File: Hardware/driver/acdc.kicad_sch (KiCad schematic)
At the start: 14 parts, among them J401 TBP02R2W-381-03BE, J402 Conn_01x02_Male

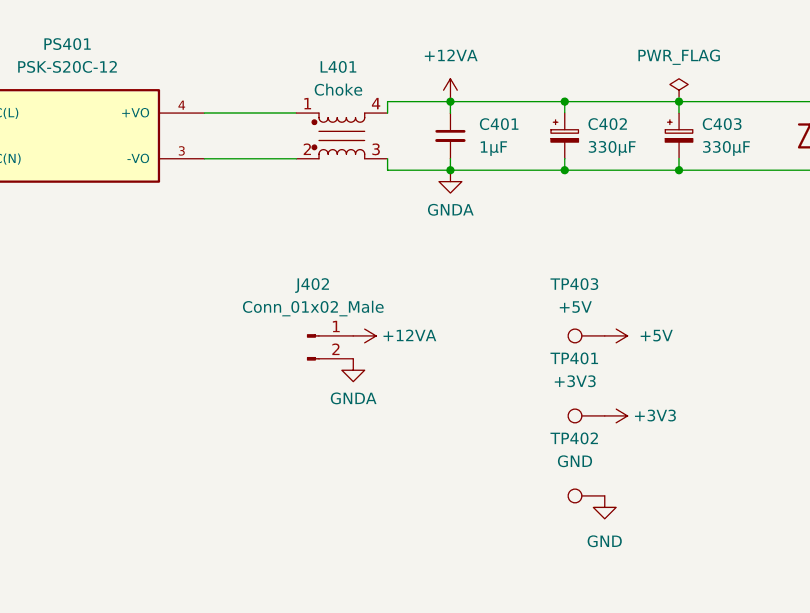
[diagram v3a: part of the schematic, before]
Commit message: Start work on remote VSense; driver board tweaks
- Use the DAC reference as the positive end of the null adjustment
  trimmers, rather than the +3V3 supply; this should make the adjustment
  actually useful and persistent rather than relying on the relationship
  between the 3V3 rail and the DAC's internal reference.

- Moved the 1Wire controller slightly to allow relocating the zero
  offset trimmer for the first channel

- Start work on remote VSense

  This works by selecting between either voltage sensing at the source
  terminals, or an external sense input connected to another set of
  terminals. These are switched by a latching relay (as to provide
  satisfying clicky noises) and then go into an op amp working as a
  differential amplifier; it performs a 50:1 gain (obviating the need
  for resistor dividers, and providing greater accuracy) and that then
  goes into the measurement ADC as normal.

  We have to still figure out how to drive the relay (probably just an
  IO expander?) and place those components on the board.
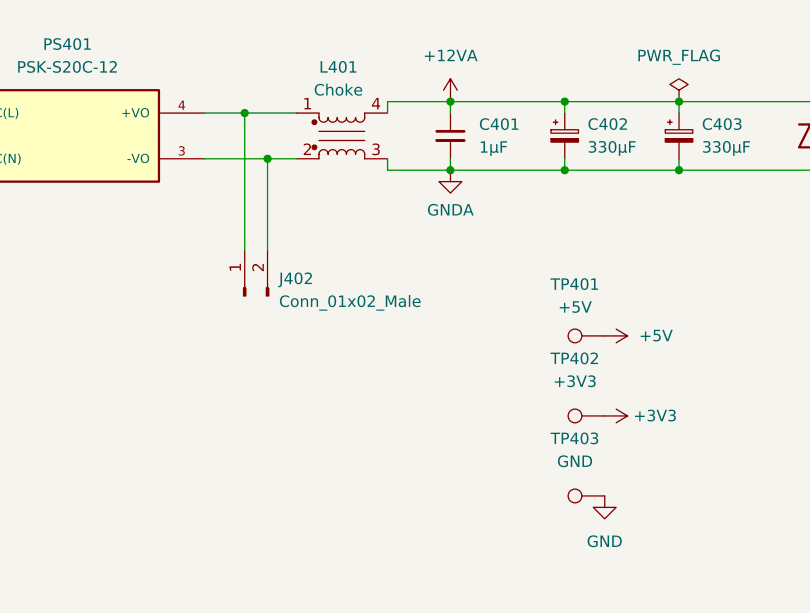
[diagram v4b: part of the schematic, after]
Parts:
- renumbered TP403 to TP401, TP401 to TP402, TP402 to TP403
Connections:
- net +12VA: no longer J402.1 (Pin_1)
- net GNDA: no longer J402.2 (Pin_2)
- net at L401.2, PS401.3 (-VO): now also J402.2 (Pin_2)
- net at L401.1, PS401.4 (+VO): now also J402.1 (Pin_1)
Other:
- moved on the sheet: J402
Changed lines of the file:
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@@
   (junction (at 140.335 45.72) (diameter 0) (color 0 0 0 0)
   )
+  (junction (at 107.315 44.45) (diameter 0) (color 0 0 0 0)
+  )
   (junction (at 52.07 46.99) (diameter 0) (color 0 0 0 0)
   )
+  (junction (at 104.775 39.37) (diameter 0) (color 0 0 0 0)
+  )
   (junction (at 140.335 38.1) (diameter 0) (color 0 0 0 0)
   )
@@
     (stroke (width 0) (type default) (color 0 0 0 0))
   )
+  (wire (pts (xy 104.775 39.37) (xy 104.775 54.61))
+    (stroke (width 0) (type default) (color 0 0 0 0))
+  )
   (wire (pts (xy 167.64 38.1) (xy 153.035 38.1))
     (stroke (width 0) (type default) (color 0 0 0 0))
@@
     (stroke (width 0) (type default) (color 0 0 0 0))
   )
+  (wire (pts (xy 104.775 39.37) (xy 110.49 39.37))
+    (stroke (width 0) (type default) (color 0 0 0 0))
+  )
   (wire (pts (xy 140.335 38.1) (xy 140.335 39.37))
     (stroke (width 0) (type default) (color 0 0 0 0))
@@
     (stroke (width 0) (type default) (color 0 0 0 0))
   )
+  (wire (pts (xy 107.315 54.61) (xy 107.315 44.45))
+    (stroke (width 0) (type default) (color 0 0 0 0))
+  )
   (wire (pts (xy 140.335 38.1) (xy 127.635 38.1))
     (stroke (width 0) (type default) (color 0 0 0 0))
@@
     (stroke (width 0) (type default) (color 0 0 0 0))
   )
-  (wire (pts (xy 100.33 39.37) (xy 110.49 39.37))
+  (wire (pts (xy 100.33 39.37) (xy 104.775 39.37))
     (stroke (width 0) (type default) (color 0 0 0 0))
   )
@@
     (stroke (width 0) (type default) (color 0 0 0 0))
   )
+  (wire (pts (xy 107.315 44.45) (xy 110.49 44.45))
+    (stroke (width 0) (type default) (color 0 0 0 0))
+  )
   (wire (pts (xy 120.65 38.1) (xy 120.65 39.37))
     (stroke (width 0) (type default) (color 0 0 0 0))
   )
-  (wire (pts (xy 100.33 44.45) (xy 110.49 44.45))
+  (wire (pts (xy 100.33 44.45) (xy 107.315 44.45))
     (stroke (width 0) (type default) (color 0 0 0 0))
   )
@@
   (symbol (lib_id "Connector:TestPoint") (at 144.78 81.915 90) (mirror x) (unit 1)
     (in_bom yes) (on_board yes) (fields_autoplaced)
-    (property "Reference" "TP402" (id 0) (at 141.478 75.565 90))
+    (property "Reference" "TP403" (id 0) (at 141.478 75.565 90))
     (property "Value" "GND" (id 1) (at 141.478 78.105 90))
     (property "Footprint" "TestPoint:TestPoint_Keystone_5000-5004_Miniature" (id 2) (at 144.78 86.995 0)
@@
   (symbol (lib_id "power:GNDA") (at 177.165 154.305 0) (unit 1)
     (in_bom yes) (on_board yes) (fields_autoplaced)
-    (property "Reference" "#PWR0117" (id 0) (at 177.165 160.655 0)
+    (property "Reference" "#PWR0406" (id 0) (at 177.165 160.655 0)
       (effects (font (size 1.27 1.27)) hide)
     )
@@
     (pin "1")
   )
-  (symbol (lib_id "Connector:Conn_01x02_Male") (at 111.76 64.135 0) (unit 1)
-    (in_bom yes) (on_board yes) (fields_autoplaced)
-    (property "Reference" "J402" (id 0) (at 112.395 58.42 0))
-    (property "Value" "Conn_01x02_Male" (id 1) (at 112.395 60.96 0))
-    (property "Footprint" "Connector_JST:JST_VH_B2P-VH-B_1x02_P3.96mm_Vertical" (id 2) (at 111.76 64.135 0)
-      (effects (font (size 1.27 1.27)) hide)
-    )
-    (property "Datasheet" "~" (id 3) (at 111.76 64.135 0)
+  (symbol (lib_id "Connector:Conn_01x02_Male") (at 104.775 59.69 90) (unit 1)
+    (in_bom yes) (on_board yes) (fields_autoplaced)
+    (property "Reference" "J402" (id 0) (at 108.585 57.7849 90)
+      (effects (font (size 1.27 1.27)) (justify right))
+    )
+    (property "Value" "Conn_01x02_Male" (id 1) (at 108.585 60.3249 90)
+      (effects (font (size 1.27 1.27)) (justify right))
+    )
+    (property "Footprint" "Connector_JST:JST_VH_B2P-VH-B_1x02_P3.96mm_Vertical" (id 2) (at 104.775 59.69 0)
+      (effects (font (size 1.27 1.27)) hide)
+    )
+    (property "Datasheet" "~" (id 3) (at 104.775 59.69 0)
       (effects (font (size 1.27 1.27)) hide)
     )
@@
   (symbol (lib_id "power:+3V3") (at 144.78 73.025 270) (unit 1)
     (in_bom yes) (on_board yes)
-    (property "Reference" "#PWR0405" (id 0) (at 140.97 73.025 0)
+    (property "Reference" "#PWR0404" (id 0) (at 140.97 73.025 0)
       (effects (font (size 1.27 1.27)) hide)
     )
@@
     (pin "2")
   )
-  (symbol (lib_id "power:+12VA") (at 116.84 64.135 270) (unit 1)
-    (in_bom yes) (on_board yes)
-    (property "Reference" "#PWR0402" (id 0) (at 113.03 64.135 0)
-      (effects (font (size 1.27 1.27)) hide)
-    )
-    (property "Value" "+12VA" (id 1) (at 120.015 64.135 90)
-      (effects (font (size 1.27 1.27)) (justify left))
-    )
-    (property "Footprint" "" (id 2) (at 116.84 64.135 0)
-      (effects (font (size 1.27 1.27)) hide)
-    )
-    (property "Datasheet" "" (id 3) (at 116.84 64.135 0)
-      (effects (font (size 1.27 1.27)) hide)
-    )
-    (pin "1")
-  )
   (symbol (lib_id "power:GND") (at 144.78 81.915 0) (unit 1)
     (in_bom yes) (on_board yes) (fields_autoplaced)
-    (property "Reference" "#PWR0406" (id 0) (at 144.78 88.265 0)
+    (property "Reference" "#PWR0405" (id 0) (at 144.78 88.265 0)
       (effects (font (size 1.27 1.27)) hide)
     )
@@
   (symbol (lib_id "power:GNDA") (at 127.635 45.72 0) (unit 1)
     (in_bom yes) (on_board yes)
-    (property "Reference" "#PWR0116" (id 0) (at 127.635 52.07 0)
+    (property "Reference" "#PWR0402" (id 0) (at 127.635 52.07 0)
       (effects (font (size 1.27 1.27)) hide)
     )
@@
   (symbol (lib_id "power:+5V") (at 144.78 64.135 270) (unit 1)
     (in_bom yes) (on_board yes) (fields_autoplaced)
-    (property "Reference" "#PWR0407" (id 0) (at 140.97 64.135 0)
+    (property "Reference" "#PWR0403" (id 0) (at 140.97 64.135 0)
       (effects (font (size 1.27 1.27)) hide)
     )
@@
   (symbol (lib_id "power:+12VA") (at 191.77 154.305 270) (unit 1)
     (in_bom yes) (on_board yes)
-    (property "Reference" "#PWR0403" (id 0) (at 187.96 154.305 0)
+    (property "Reference" "#PWR0407" (id 0) (at 187.96 154.305 0)
       (effects (font (size 1.27 1.27)) hide)
     )
@@
   (symbol (lib_id "Connector:TestPoint") (at 144.78 73.025 90) (mirror x) (unit 1)
     (in_bom yes) (on_board yes) (fields_autoplaced)
-    (property "Reference" "TP401" (id 0) (at 141.478 66.675 90))
+    (property "Reference" "TP402" (id 0) (at 141.478 66.675 90))
     (property "Value" "+3V3" (id 1) (at 141.478 69.215 90))
     (property "Footprint" "TestPoint:TestPoint_Keystone_5000-5004_Miniature" (id 2) (at 144.78 78.105 0)
@@
     )
     (property "MPN" "5000" (id 5) (at 144.78 73.025 0)
-      (effects (font (size 1.27 1.27)) hide)
-    )
-    (pin "1")
-  )
-  (symbol (lib_id "power:GNDA") (at 116.84 66.675 0) (unit 1)
-    (in_bom yes) (on_board yes)
-    (property "Reference" "#PWR0404" (id 0) (at 116.84 73.025 0)
-      (effects (font (size 1.27 1.27)) hide)
-    )
-    (property "Value" "GNDA" (id 1) (at 116.84 71.12 0))
-    (property "Footprint" "" (id 2) (at 116.84 66.675 0)
-      (effects (font (size 1.27 1.27)) hide)
-    )
-    (property "Datasheet" "" (id 3) (at 116.84 66.675 0)
       (effects (font (size 1.27 1.27)) hide)
     )
@@
   (symbol (lib_id "Connector:TestPoint") (at 144.78 64.135 90) (mirror x) (unit 1)
     (in_bom yes) (on_board yes) (fields_autoplaced)
-    (property "Reference" "TP403" (id 0) (at 141.478 58.42 90))
+    (property "Reference" "TP401" (id 0) (at 141.478 58.42 90))
     (property "Value" "+5V" (id 1) (at 141.478 60.96 90))
     (property "Footprint" "TestPoint:TestPoint_Keystone_5000-5004_Miniature" (id 2) (at 144.78 69.215 0)

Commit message: Begin rev2 of driver board
- Improve the power side of things to provide +15V, +12V, +5V, +3V3, and
  -5V on the isolated side of the driver board. This is needed so that
  we can have the +12V for driving opamps with wider swing for the
  drive MOSFETs; these will not turn on with 3V3 as in the original rev1
  design so new driver op amps (U302, U306) need to be chosen
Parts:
- added TP404: (no value), TestPoint:TestPoint_Keystone_5000-5004_Miniature, symbol Connector:TestPoint
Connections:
- new net +15V: TP404.1
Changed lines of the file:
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@@
   (title_block
     (title "Dual Programmable Load Driver")
-    (date "2022-03-10")
-    (rev "1")
+    (date "2022-04-01")
+    (rev "2")
     (comment 1 "AC/DC mains supply to generate 12V")
     (comment 2 "Omit all components (except D402, R401) if not using built in mains switching supply")
@@
     (pin "3")
   )
+  (symbol (lib_id "power:+15V") (at 144.78 96.52 270) (unit 1)
+    (in_bom yes) (on_board yes) (fields_autoplaced)
+    (property "Reference" "#PWR0408" (id 0) (at 140.97 96.52 0)
+      (effects (font (size 1.27 1.27)) hide)
+    )
+    (property "Value" "" (id 1) (at 148.59 96.5199 90)
+      (effects (font (size 1.27 1.27)) (justify left))
+    )
+    (property "Footprint" "" (id 2) (at 144.78 96.52 0)
+      (effects (font (size 1.27 1.27)) hide)
+    )
+    (property "Datasheet" "" (id 3) (at 144.78 96.52 0)
+      (effects (font (size 1.27 1.27)) hide)
+    )
+    (pin "1")
+  )
   (symbol (lib_id "power:+12VA") (at 127.635 38.1 0) (unit 1)
     (in_bom yes) (on_board yes) (fields_autoplaced)
@@
     (pin "2")
   )
+  (symbol (lib_id "Connector:TestPoint") (at 144.78 96.52 90) (mirror x) (unit 1)
+    (in_bom yes) (on_board yes) (fields_autoplaced)
+    (property "Reference" "TP404" (id 0) (at 141.478 90.17 90))
+    (property "Value" "" (id 1) (at 141.478 92.71 90))
+    (property "Footprint" "TestPoint:TestPoint_Keystone_5000-5004_Miniature" (id 2) (at 144.78 101.6 0)
+      (effects (font (size 1.27 1.27)) hide)
+    )
+    (property "Datasheet" "~" (id 3) (at 144.78 101.6 0)
+      (effects (font (size 1.27 1.27)) hide)
+    )
+    (property "Color" "Red" (id 4) (at 144.78 96.52 0)
+      (effects (font (size 1.27 1.27)) hide)
+    )
+    (property "MPN" "5000" (id 5) (at 144.78 96.52 0)
+      (effects (font (size 1.27 1.27)) hide)
+    )
+    (pin "1")
+  )
   (symbol (lib_id "Connector:TestPoint") (at 144.78 64.135 90) (mirror x) (unit 1)

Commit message: More rev 2 driver board work
- Updated power supply section with linear regulators for the +12V and
  +5V rails

- Replaced op amps for driving the MOSFETs with different ones, and
  updated them so that they actually run off the 12V rail instead of the
  3V3 rail.
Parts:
- added TP405: (no value), TestPoint:TestPoint_Keystone_5000-5004_Miniature, symbol Connector:TestPoint
- TP404: value (none) -> +15V
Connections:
- new net +12V: TP405.1
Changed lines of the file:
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@@
     (pin "4")
+  )
+  (symbol (lib_id "Connector:TestPoint") (at 144.78 106.045 90) (mirror x) (unit 1)
+    (in_bom yes) (on_board yes) (fields_autoplaced)
+    (property "Reference" "TP405" (id 0) (at 141.478 100.33 90))
+    (property "Value" "" (id 1) (at 141.478 102.87 90))
+    (property "Footprint" "TestPoint:TestPoint_Keystone_5000-5004_Miniature" (id 2) (at 144.78 111.125 0)
+      (effects (font (size 1.27 1.27)) hide)
+    )
+    (property "Datasheet" "~" (id 3) (at 144.78 111.125 0)
+      (effects (font (size 1.27 1.27)) hide)
+    )
+    (property "Color" "Red" (id 4) (at 144.78 106.045 0)
+      (effects (font (size 1.27 1.27)) hide)
+    )
+    (property "MPN" "5000" (id 5) (at 144.78 106.045 0)
+      (effects (font (size 1.27 1.27)) hide)
+    )
+    (pin "1")
   )
   (symbol (lib_id "power:GNDA") (at 177.165 154.305 0) (unit 1)
@@
     (pin "2")
   )
+  (symbol (lib_id "power:+12V") (at 144.78 106.045 270) (unit 1)
+    (in_bom yes) (on_board yes) (fields_autoplaced)
+    (property "Reference" "#PWR0128" (id 0) (at 140.97 106.045 0)
+      (effects (font (size 1.27 1.27)) hide)
+    )
+    (property "Value" "" (id 1) (at 148.59 106.0449 90)
+      (effects (font (size 1.27 1.27)) (justify left))
+    )
+    (property "Footprint" "" (id 2) (at 144.78 106.045 0)
+      (effects (font (size 1.27 1.27)) hide)
+    )
+    (property "Datasheet" "" (id 3) (at 144.78 106.045 0)
+      (effects (font (size 1.27 1.27)) hide)
+    )
+    (pin "1")
+  )
   (symbol (lib_id "Connector:TestPoint") (at 144.78 73.025 90) (mirror x) (unit 1)
     (in_bom yes) (on_board yes) (fields_autoplaced)
@@
       (effects (font (size 1.27 1.27)) hide)
     )
-    (property "Value" "" (id 1) (at 148.59 96.5199 90)
+    (property "Value" "+15V" (id 1) (at 148.59 96.5199 90)
       (effects (font (size 1.27 1.27)) (justify left))
     )
@@
     (in_bom yes) (on_board yes) (fields_autoplaced)
     (property "Reference" "TP404" (id 0) (at 141.478 90.17 90))
-    (property "Value" "" (id 1) (at 141.478 92.71 90))
+    (property "Value" "+15V" (id 1) (at 141.478 92.71 90))
     (property "Footprint" "TestPoint:TestPoint_Keystone_5000-5004_Miniature" (id 2) (at 144.78 101.6 0)
       (effects (font (size 1.27 1.27)) hide)

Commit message: More work on rev2 driver board
- Tweaked the board layout for the load driver some more, primarily
  relating to power and friends

- Fixed footprint of fan connector on driver board (to properly have the
  mechanical mounting hole)

- Manufacturability/solderability tweaks for a few other footprints
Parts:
- TP405: value (none) -> +12V
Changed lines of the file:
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@@
     (in_bom yes) (on_board yes) (fields_autoplaced)
     (property "Reference" "TP405" (id 0) (at 141.478 100.33 90))
-    (property "Value" "" (id 1) (at 141.478 102.87 90))
+    (property "Value" "+12V" (id 1) (at 141.478 102.87 90))
     (property "Footprint" "TestPoint:TestPoint_Keystone_5000-5004_Miniature" (id 2) (at 144.78 111.125 0)
       (effects (font (size 1.27 1.27)) hide)
@@
       (effects (font (size 1.27 1.27)) hide)
     )
-    (property "Value" "" (id 1) (at 148.59 106.0449 90)
-      (effects (font (size 1.27 1.27)) (justify left))
-    )
+    (property "Value" "+12V" (id 1) (at 148.59 106.0449 90)
+      (effects (font (size 1.27 1.27)) (justify left))
+    )

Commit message: Add some missing part numbers to analog board
- Some components on analog load were missing part numbers, so this adds
  them. It also fixes a few components with the same value, where some
  had a part number and others didn't.
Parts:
- C401: value 1µF -> (none); footprint Capacitor_SMD:C_0805_2012Metric_Pad1.18x1.45mm_HandSolder -> (none); MPN 187-CL21B105KBFNNNG -> CL21B105KBFNNNG
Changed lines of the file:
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@@
       (effects (font (size 1.27 1.27)) (justify left))
     )
-    (property "Value" "1µF" (id 1) (at 130.81 43.1862 0)
+    (property "Value" "" (id 1) (at 130.81 43.1862 0)
       (effects (font (size 1.27 1.27)) (justify left))
     )
-    (property "Footprint" "Capacitor_SMD:C_0805_2012Metric_Pad1.18x1.45mm_HandSolder" (id 2) (at 127.635 41.91 0)
+    (property "Footprint" "" (id 2) (at 127.635 41.91 0)
       (effects (font (size 1.27 1.27)) hide)
     )
@@
       (effects (font (size 1.27 1.27)) hide)
     )
-    (property "MPN" "187-CL21B105KBFNNNG" (id 4) (at 127.635 41.91 0)
+    (property "MPN" "CL21B105KBFNNNG" (id 4) (at 127.635 41.91 0)
       (effects (font (size 1.27 1.27)) hide)
     )
